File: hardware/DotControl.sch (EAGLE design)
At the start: 43 parts, among them CN1 1X4-BIG, J3 USB-MICROB, SW2 Previous, SW5 Previous, SW6 Next, SW8 Ok, U1 ATMEGA328P-MU-QFN32, U2 TMP102, U3 ATSHA204-TSU, U4 SI7021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

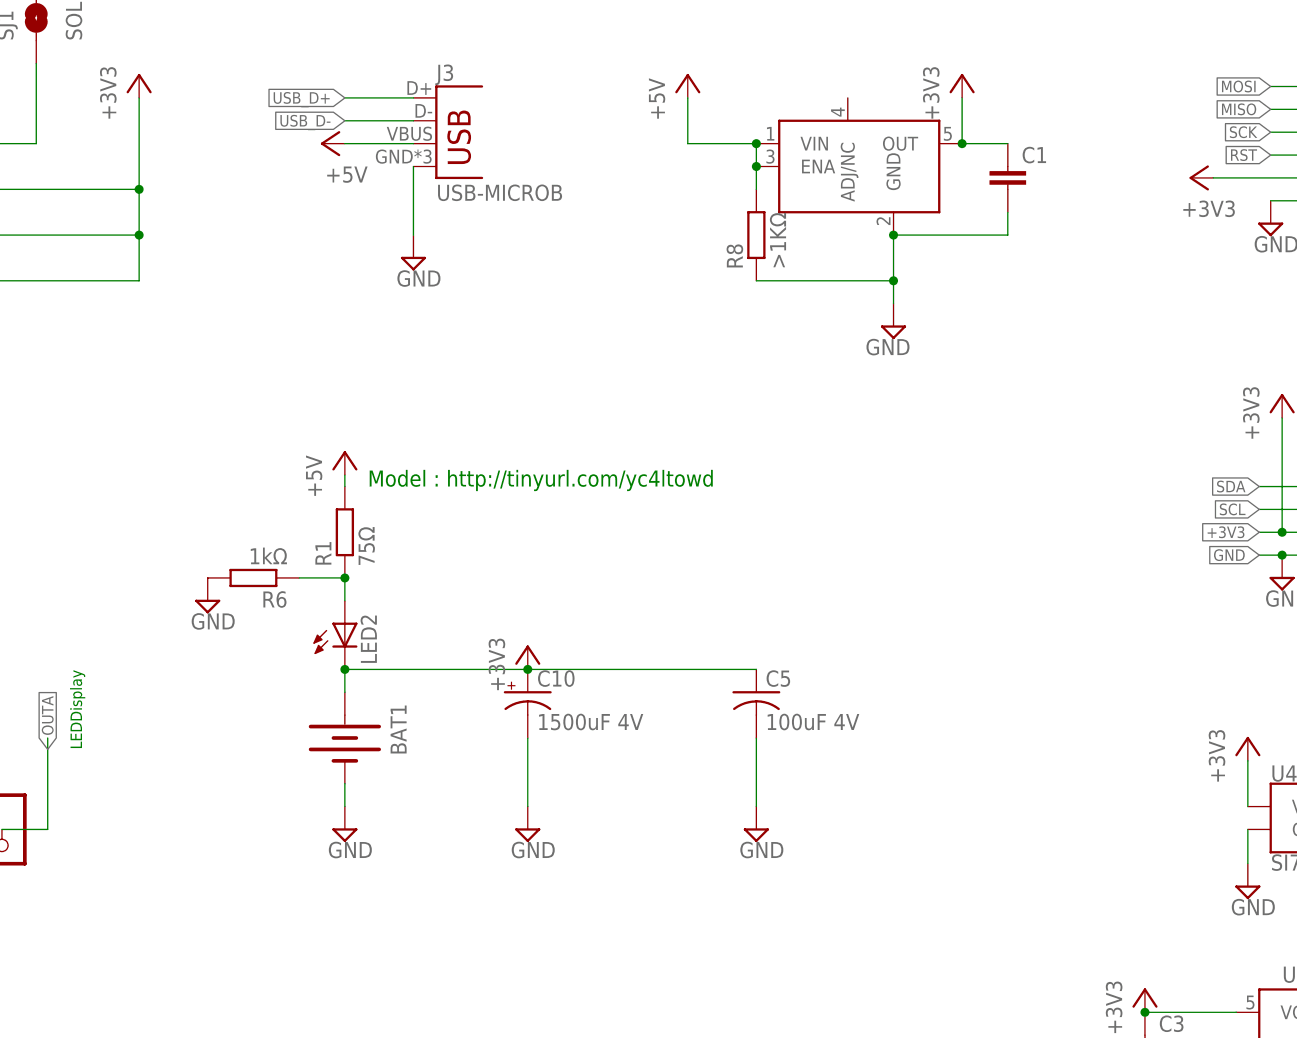
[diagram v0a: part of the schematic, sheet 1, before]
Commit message: [Intermediate] Improve coincell charging
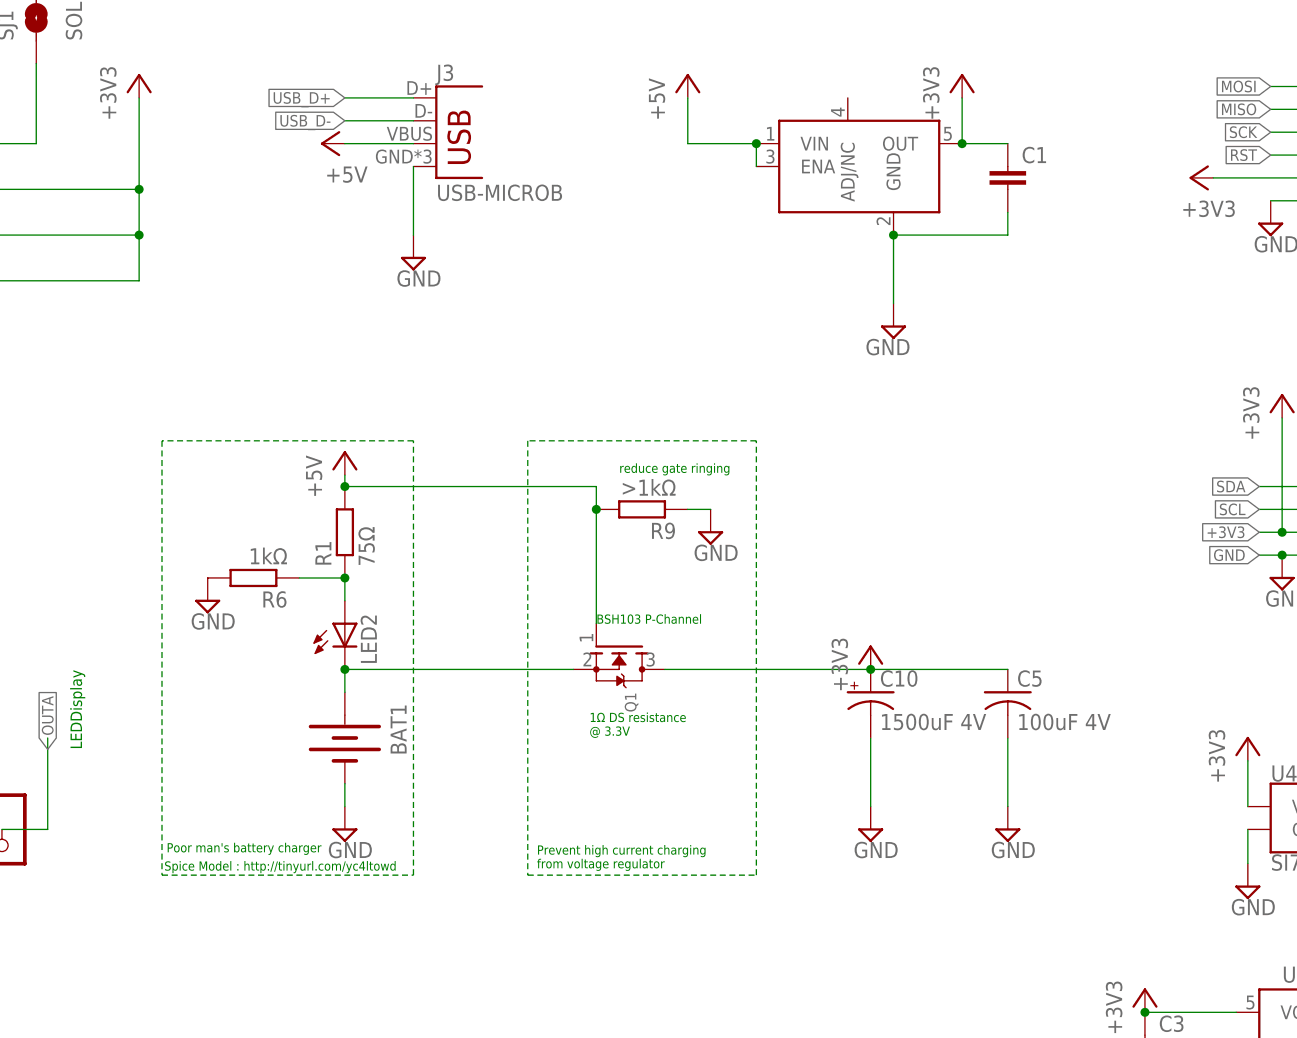
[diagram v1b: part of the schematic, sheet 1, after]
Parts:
- removed R8: >1KΩ, resistor:R-EU_R0603
- added Q1: (no value), adafruit:MOSFET-NREFLOW
- added R9: >1kΩ, resistor:R-EU_R0603
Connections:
- new net N$18: BAT1.+, LED2.C, Q1.S
- net +3V3: now also Q1.D; no longer BAT1.+, LED2.C
- net +5V: now also Q1.G, R9.2; no longer R8.2
- net GND: now also R9.1; no longer R8.1
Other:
- note added: "1Ω DS resistance @ 3.3V"
- note added: "BSH103 P-Channel"
- note added: "Poor man's battery charger"
- note added: "Prevent high current charging from voltage regulator"
- note added: "Spice Model : http://tinyurl.com/yc4ltowd"
- note added: "reduce gate ringing"
- note removed: "Model : http://tinyurl.com/yc4ltowd"
- moved on the sheet: C10, C5
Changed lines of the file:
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@@
 <setting verticaltext="up"/>
 </settings>
-<grid distance="0.1" unitdist="inch" unit="inch" style="lines" multiple="1" display="no" altdistance="0.01" altunitdist="inch" altunit="inch"/>
+<grid distance="0.01" unitdist="inch" unit="inch" style="lines" multiple="1" display="no" altdistance="0.01" altunitdist="inch" altunit="inch"/>
 <layers>
 <layer number="1" name="Top" color="4" fill="1" visible="no" active="no"/>
@@
 <part name="C5" library="adafruit" deviceset="C-US" device="C3216" value="100uF 4V"/>
 <part name="SUPPLY21" library="supply2" deviceset="GND" device=""/>
-<part name="R8" library="resistor" deviceset="R-EU_" device="R0603" value="&gt;1KΩ"/>
+<part name="R9" library="resistor" deviceset="R-EU_" device="R0603" value="&gt;1kΩ"/>
+<part name="SUPPLY22" library="supply2" deviceset="GND" device=""/>
+<part name="Q1" library="adafruit" deviceset="MOSFET-N" device="REFLOW"/>
 </parts>
 <sheets>
@@
 <text x="505.46" y="167.64" size="3.81" layer="95">Movement</text>
 <wire x1="457.2" y1="246.38" x2="457.2" y2="165.1" width="0.1524" layer="95" style="longdash"/>
-<text x="116.84" y="167.64" size="1.778" layer="91">Model : http://tinyurl.com/yc4ltowd</text>
+<text x="94.234" y="124.968" size="1.016" layer="91">Spice Model : http://tinyurl.com/yc4ltowd</text>
+<text x="142.24" y="152.4" size="1.016" layer="91">BSH103 P-Channel</text>
+<text x="94.488" y="127" size="1.016" layer="91">Poor man's battery charger</text>
+<text x="135.636" y="125.222" size="1.016" layer="91">Prevent high current charging
+from voltage regulator</text>
+<text x="144.78" y="169.164" size="1.016" layer="91">reduce gate ringing</text>
+<text x="141.478" y="139.954" size="1.016" layer="91">1Ω DS resistance
+@ 3.3V</text>
 </plain>
 <instances>
@@
 <instance part="SUPPLY5" gate="GND" x="228.6" y="53.34"/>
 <instance part="SJ2" gate="1" x="217.17" y="34.29" rot="R180"/>
-<instance part="+3V9" gate="G$1" x="134.62" y="149.86"/>
+<instance part="+3V9" gate="G$1" x="172.72" y="149.86"/>
 <instance part="D1" gate="G$1" x="322.58" y="99.06" rot="R90"/>
 <instance part="D2" gate="G$1" x="332.74" y="99.06" rot="R90"/>
@@
 <instance part="+3V12" gate="G$1" x="214.63" y="139.7"/>
 <instance part="SUPPLY11" gate="GND" x="214.63" y="123.19"/>
-<instance part="C10" gate="G$1" x="134.62" y="144.78"/>
-<instance part="SUPPLY16" gate="GND" x="134.62" y="129.54"/>
+<instance part="C10" gate="G$1" x="172.72" y="144.78"/>
+<instance part="SUPPLY16" gate="GND" x="172.72" y="129.54"/>
 <instance part="U5" gate="G$1" x="525.78" y="220.98"/>
 <instance part="SUPPLY23" gate="GND" x="508" y="213.36"/>
@@
 <instance part="R6" gate="G$1" x="104.14" y="157.48" rot="R180"/>
 <instance part="SUPPLY20" gate="GND" x="99.06" y="154.94"/>
-<instance part="C5" gate="G$1" x="160.02" y="144.78"/>
-<instance part="SUPPLY21" gate="GND" x="160.02" y="129.54"/>
-<instance part="R8" gate="G$1" x="160.02" y="195.58" rot="R90"/>
+<instance part="C5" gate="G$1" x="187.96" y="144.78"/>
+<instance part="SUPPLY21" gate="GND" x="187.96" y="129.54"/>
+<instance part="R9" gate="G$1" x="147.32" y="165.1" rot="R180"/>
+<instance part="SUPPLY22" gate="GND" x="154.94" y="162.56"/>
+<instance part="Q1" gate="G$1" x="144.78" y="149.86" rot="R270"/>
 </instances>
 <busses>
@@
 <pinref part="U$4" gate="G$1" pin="GND"/>
 <pinref part="SUPPLY27" gate="GND" pin="GND"/>
-<wire x1="175.26" y1="187.96" x2="175.26" y2="190.5" width="0.1524" layer="91"/>
 <pinref part="C1" gate="G$1" pin="2"/>
-<wire x1="175.26" y1="190.5" x2="175.26" y2="195.58" width="0.1524" layer="91"/>
+<wire x1="175.26" y1="187.96" x2="175.26" y2="195.58" width="0.1524" layer="91"/>
 <wire x1="175.26" y1="195.58" x2="187.96" y2="195.58" width="0.1524" layer="91"/>
 <wire x1="187.96" y1="195.58" x2="187.96" y2="198.12" width="0.1524" layer="91"/>
 <junction x="175.26" y="195.58"/>
-<pinref part="R8" gate="G$1" pin="1"/>
-<wire x1="160.02" y1="190.5" x2="175.26" y2="190.5" width="0.1524" layer="91"/>
-<junction x="175.26" y="190.5"/>
 </segment>
 <segment>
@@
 <pinref part="C10" gate="G$1" pin="-"/>
 <pinref part="SUPPLY16" gate="GND" pin="GND"/>
-<wire x1="134.62" y1="139.7" x2="134.62" y2="132.08" width="0.1524" layer="91"/>
+<wire x1="172.72" y1="139.7" x2="172.72" y2="132.08" width="0.1524" layer="91"/>
 </segment>
 <segment>
@@
 <pinref part="C5" gate="G$1" pin="2"/>
 <pinref part="SUPPLY21" gate="GND" pin="GND"/>
-<wire x1="160.02" y1="139.7" x2="160.02" y2="132.08" width="0.1524" layer="91"/>
+<wire x1="187.96" y1="139.7" x2="187.96" y2="132.08" width="0.1524" layer="91"/>
+</segment>
+<segment>
+<pinref part="SUPPLY22" gate="GND" pin="GND"/>
+<pinref part="R9" gate="G$1" pin="1"/>
+<wire x1="154.94" y1="165.1" x2="152.4" y2="165.1" width="0.1524" layer="91"/>
 </segment>
 </net>
@@
 </segment>
 <segment>
-<pinref part="LED2" gate="G$1" pin="C"/>
-<pinref part="BAT1" gate="G$1" pin="+"/>
-<wire x1="114.3" y1="147.32" x2="114.3" y2="144.78" width="0.1524" layer="91"/>
 <pinref part="+3V9" gate="G$1" pin="+3V3"/>
-<wire x1="134.62" y1="147.32" x2="114.3" y2="147.32" width="0.1524" layer="91"/>
-<junction x="114.3" y="147.32"/>
 <pinref part="C10" gate="G$1" pin="+"/>
-<junction x="134.62" y="147.32"/>
+<junction x="172.72" y="147.32"/>
 <pinref part="C5" gate="G$1" pin="1"/>
-<wire x1="134.62" y1="147.32" x2="160.02" y2="147.32" width="0.1524" layer="91"/>
+<wire x1="172.72" y1="147.32" x2="187.96" y2="147.32" width="0.1524" layer="91"/>
+<wire x1="149.86" y1="147.32" x2="172.72" y2="147.32" width="0.1524" layer="91"/>
+<pinref part="Q1" gate="G$1" pin="D"/>
 </segment>
 <segment>
@@
 <wire x1="160.02" y1="203.2" x2="160.02" y2="205.74" width="0.1524" layer="91"/>
 <junction x="160.02" y="205.74"/>
-<pinref part="R8" gate="G$1" pin="2"/>
-<junction x="160.02" y="203.2"/>
-<wire x1="160.02" y1="203.2" x2="160.02" y2="200.66" width="0.1524" layer="91"/>
 </segment>
 <segment>
@@
 <wire x1="114.3" y1="167.64" x2="114.3" y2="168.91" width="0.1524" layer="91"/>
 <pinref part="P+5" gate="1" pin="+5V"/>
+<pinref part="R9" gate="G$1" pin="2"/>
+<wire x1="142.24" y1="165.1" x2="142.24" y2="152.4" width="0.1524" layer="91"/>
+<wire x1="142.24" y1="165.1" x2="142.24" y2="167.64" width="0.1524" layer="91"/>
+<wire x1="142.24" y1="167.64" x2="114.3" y2="167.64" width="0.1524" layer="91"/>
+<junction x="142.24" y="165.1"/>
+<junction x="114.3" y="167.64"/>
+<pinref part="Q1" gate="G$1" pin="G"/>
 </segment>
 <segment>
@@
 </segment>
 </net>
+<net name="N$18" class="0">
+<segment>
+<pinref part="BAT1" gate="G$1" pin="+"/>
+<pinref part="LED2" gate="G$1" pin="C"/>
+<wire x1="114.3" y1="147.32" x2="114.3" y2="144.78" width="0.1524" layer="91"/>
+<wire x1="139.7" y1="147.32" x2="114.3" y2="147.32" width="0.1524" layer="91"/>
+<junction x="114.3" y="147.32"/>
+<pinref part="Q1" gate="G$1" pin="S"/>
+</segment>
+</net>
+<net name="N$17" class="0">
+<segment>
+<wire x1="121.92" y1="172.72" x2="93.98" y2="172.72" width="0.1524" layer="91" style="shortdash"/>
+<wire x1="93.98" y1="172.72" x2="93.98" y2="124.46" width="0.1524" layer="91" style="shortdash"/>
+<wire x1="93.98" y1="124.46" x2="121.92" y2="124.46" width="0.1524" layer="91" style="shortdash"/>
+<wire x1="121.92" y1="124.46" x2="121.92" y2="172.72" width="0.1524" layer="91" style="shortdash"/>
+</segment>
+</net>
+<net name="N$19" class="0">
+<segment>
+<wire x1="134.62" y1="172.72" x2="134.62" y2="124.46" width="0.1524" layer="91" style="shortdash"/>
+<wire x1="134.62" y1="124.46" x2="160.02" y2="124.46" width="0.1524" layer="91" style="shortdash"/>
+<wire x1="160.02" y1="124.46" x2="160.02" y2="172.72" width="0.1524" layer="91" style="shortdash"/>
+<wire x1="160.02" y1="172.72" x2="134.62" y2="172.72" width="0.1524" layer="91" style="shortdash"/>
+</segment>
+</net>

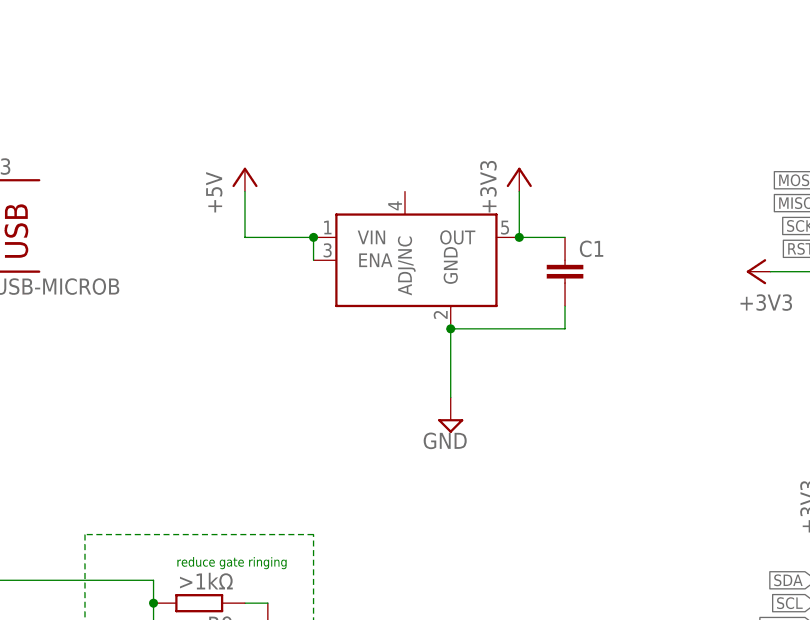
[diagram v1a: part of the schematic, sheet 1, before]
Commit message: Replace LDO with low quiescence regulator
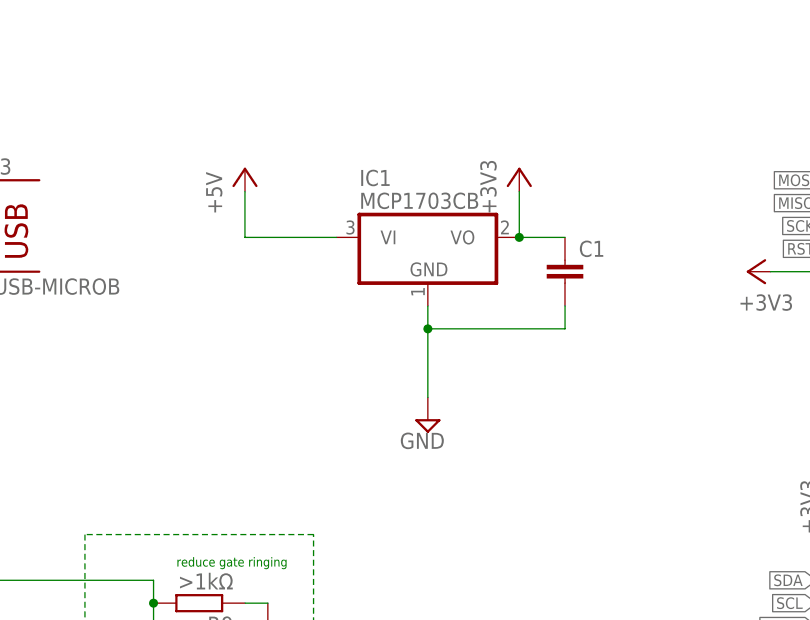
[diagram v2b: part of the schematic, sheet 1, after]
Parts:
- removed U$4: LDCL015, LDCL015:LDCL015
- added IC1: MCP1703CB, linear:MCP1703CB
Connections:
- net +3V3: now also IC1.VO; no longer U$4.OUT
- net +5V: now also IC1.VI; no longer U$4.ENA, U$4.VIN
- net GND: now also IC1.GND; no longer U$4.GND
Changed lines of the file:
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@@
 <setting verticaltext="up"/>
 </settings>
-<grid distance="0.01" unitdist="inch" unit="inch" style="lines" multiple="1" display="no" altdistance="0.01" altunitdist="inch" altunit="inch"/>
+<grid distance="0.1" unitdist="inch" unit="inch" style="lines" multiple="1" display="no" altdistance="0.01" altunitdist="inch" altunit="inch"/>
 <layers>
 <layer number="1" name="Top" color="4" fill="1" visible="no" active="no"/>
@@
 <part name="SUPPLY10" library="supply2" deviceset="GND" device=""/>
 <part name="J3" library="SparkFun-Retired" deviceset="USB" device="-MICROB"/>
-<part name="U$4" library="LDCL015" deviceset="LDCL015" device=""/>
 <part name="SUPPLY27" library="supply2" deviceset="GND" device=""/>
 <part name="+3V19" library="supply1" deviceset="+3V3" device=""/>
@@
 <part name="SUPPLY22" library="supply2" deviceset="GND" device=""/>
 <part name="Q1" library="adafruit" deviceset="MOSFET-N" device="REFLOW"/>
+<part name="IC1" library="linear" deviceset="MCP1703" device="CB"/>
 </parts>
 <sheets>
@@
 <instance part="SUPPLY10" gate="GND" x="121.92" y="193.04"/>
 <instance part="J3" gate="G$1" x="124.46" y="203.2"/>
-<instance part="U$4" gate="G$1" x="170.18" y="203.2"/>
-<instance part="SUPPLY27" gate="GND" x="175.26" y="185.42" rot="MR0"/>
+<instance part="SUPPLY27" gate="GND" x="172.72" y="185.42" rot="MR0"/>
 <instance part="+3V19" gate="G$1" x="182.88" y="213.36"/>
 <instance part="P+4" gate="1" x="152.4" y="213.36"/>
@@
 <instance part="SUPPLY22" gate="GND" x="154.94" y="162.56"/>
 <instance part="Q1" gate="G$1" x="144.78" y="149.86" rot="R270"/>
+<instance part="IC1" gate="G$1" x="172.72" y="205.74"/>
 </instances>
 <busses>
@@
 </segment>
 <segment>
-<pinref part="U$4" gate="G$1" pin="GND"/>
 <pinref part="SUPPLY27" gate="GND" pin="GND"/>
 <pinref part="C1" gate="G$1" pin="2"/>
-<wire x1="175.26" y1="187.96" x2="175.26" y2="195.58" width="0.1524" layer="91"/>
-<wire x1="175.26" y1="195.58" x2="187.96" y2="195.58" width="0.1524" layer="91"/>
+<wire x1="172.72" y1="187.96" x2="172.72" y2="195.58" width="0.1524" layer="91"/>
+<wire x1="172.72" y1="195.58" x2="187.96" y2="195.58" width="0.1524" layer="91"/>
 <wire x1="187.96" y1="195.58" x2="187.96" y2="198.12" width="0.1524" layer="91"/>
-<junction x="175.26" y="195.58"/>
+<pinref part="IC1" gate="G$1" pin="GND"/>
+<wire x1="172.72" y1="198.12" x2="172.72" y2="195.58" width="0.1524" layer="91"/>
+<junction x="172.72" y="195.58"/>
 </segment>
 <segment>
@@
 </segment>
 <segment>
-<pinref part="U$4" gate="G$1" pin="OUT"/>
 <pinref part="+3V19" gate="G$1" pin="+3V3"/>
 <wire x1="182.88" y1="210.82" x2="182.88" y2="205.74" width="0.1524" layer="91"/>
 <pinref part="C1" gate="G$1" pin="1"/>
 <wire x1="187.96" y1="205.74" x2="182.88" y2="205.74" width="0.1524" layer="91"/>
+<pinref part="IC1" gate="G$1" pin="VO"/>
 <junction x="182.88" y="205.74"/>
 </segment>
@@
 <segment>
 <pinref part="P+4" gate="1" pin="+5V"/>
-<pinref part="U$4" gate="G$1" pin="VIN"/>
 <wire x1="152.4" y1="210.82" x2="152.4" y2="205.74" width="0.1524" layer="91"/>
-<wire x1="152.4" y1="205.74" x2="160.02" y2="205.74" width="0.1524" layer="91"/>
-<pinref part="U$4" gate="G$1" pin="ENA"/>
-<wire x1="160.02" y1="203.2" x2="160.02" y2="205.74" width="0.1524" layer="91"/>
-<junction x="160.02" y="205.74"/>
-</segment>
-<segment>
+<wire x1="152.4" y1="205.74" x2="162.56" y2="205.74" width="0.1524" layer="91"/>
+<pinref part="IC1" gate="G$1" pin="VI"/>
+</segment>
+<segment>
